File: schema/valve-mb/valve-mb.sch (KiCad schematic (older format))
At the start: 13 parts

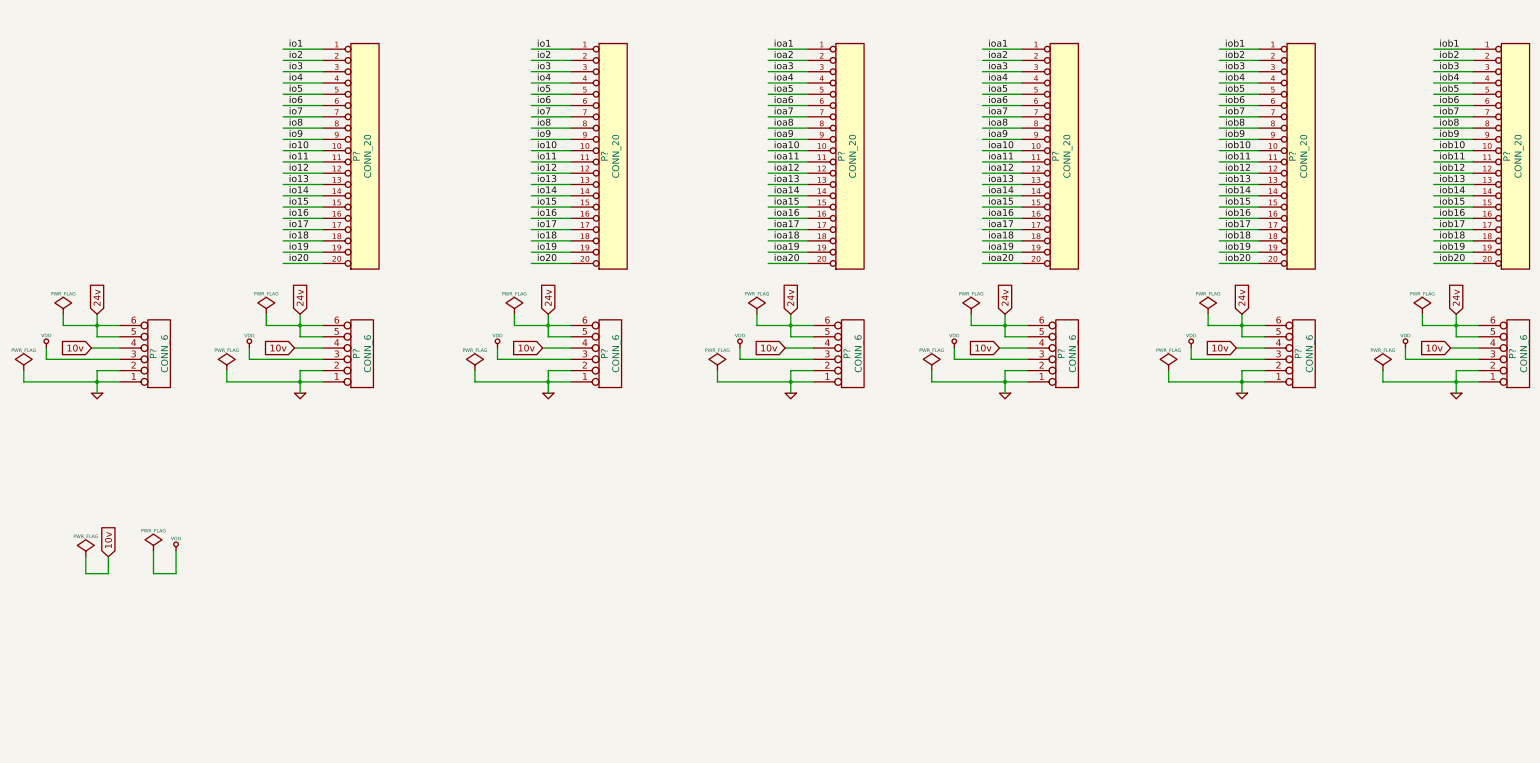
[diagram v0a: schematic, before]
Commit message: Разведена плата с разъёмами для объединения функциональных плат.
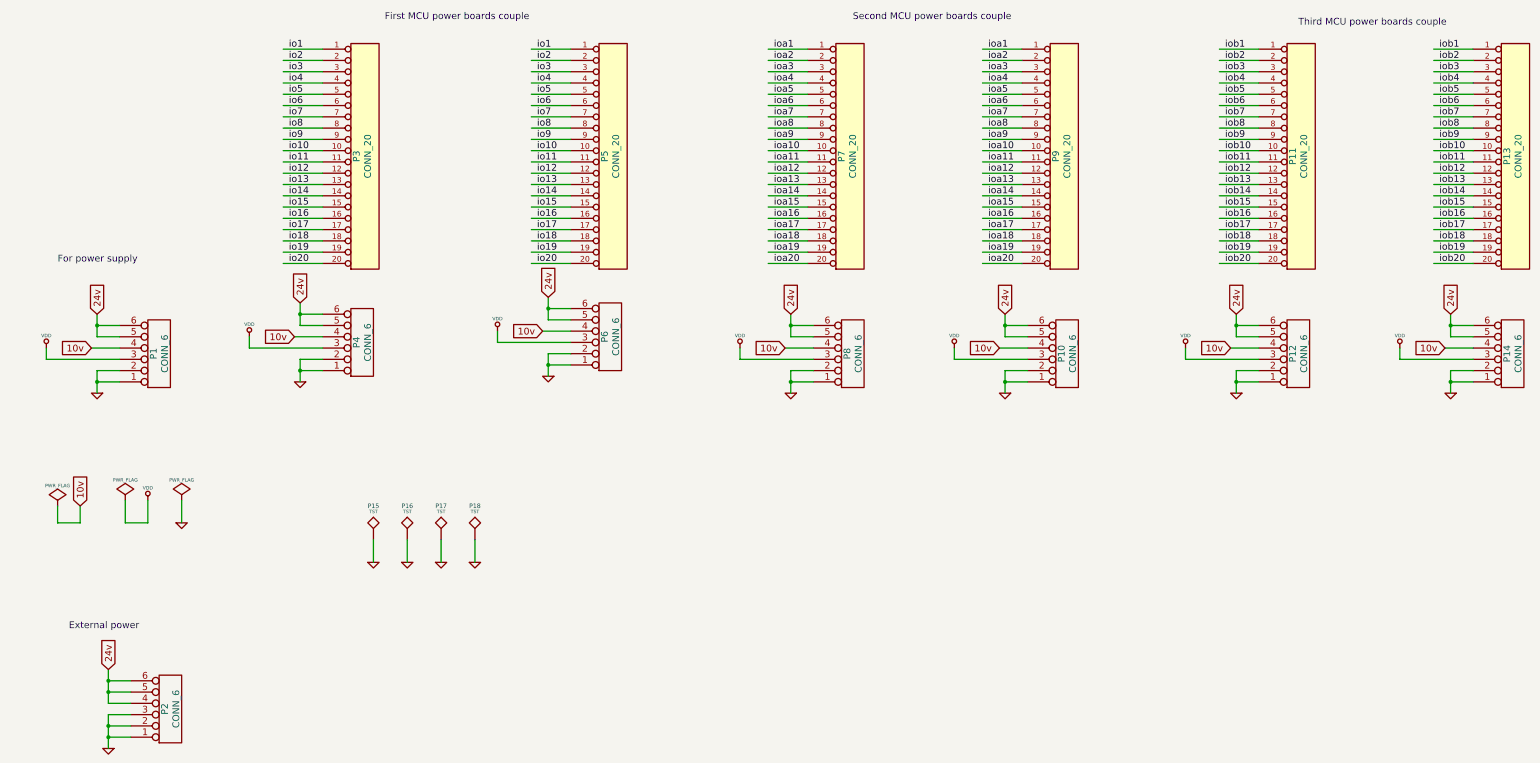
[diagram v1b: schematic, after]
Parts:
- removed P? (x6): CONN_6, symbol CONN_6
- added P10, P12, P14, P2, P4, P6, P8: CONN_6, symbol CONN_6
- added P15, P16, P17, P18: TST, symbol TST
- gave numbers to parts that had none: 7
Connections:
- wire segments 203 -> 202
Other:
- note added: "External power"
- note added: "First MCU power boards couple"
- note added: "For power supply"
- note added: "Second MCU power boards couple"
- note added: "Third MCU power boards couple"
